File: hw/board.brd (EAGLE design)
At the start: 50 x 50 mm, 21 parts, among them IC2 HS73XX, IC3 DS1820, IC4 DS1820

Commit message: Changes to the board
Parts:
- moved +3.3V 8.89 mm to (2.54, 36.2)
- moved C3 6.35 mm to (5.71, 28.6)
- moved MOTOR 6.35 mm to (2.54, 28.6)
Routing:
- net +3V3: track 143.0 -> 150.0 mm
- net 1Y: track 19.0 -> 24.1 mm
- net 2Y: track 19.0 -> 15.9 mm
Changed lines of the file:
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@@
 <?xml version="1.0" encoding="utf-8"?>
 <!DOCTYPE eagle SYSTEM "eagle.dtd">
-<eagle version="6.6.0">
+<eagle version="7.0.0">
 <drawing>
 <settings>
@@
 <text x="41.91" y="34.925" size="0.8128" layer="25" font="vector" ratio="15" rot="R180" align="center-left">SCL</text>
 <hole x="1.905" y="1.905" drill="2.8"/>
-<text x="4.445" y="26.035" size="0.8128" layer="25" font="vector" ratio="15" align="center-left">+3.3V</text>
-<text x="4.445" y="28.575" size="0.8128" layer="25" font="vector" ratio="15" align="center-left">GND</text>
+<text x="4.445" y="34.925" size="0.8128" layer="25" font="vector" ratio="15" align="center-left">+3.3V</text>
+<text x="4.445" y="37.465" size="0.8128" layer="25" font="vector" ratio="15" align="center-left">GND</text>
 <text x="4.445" y="44.45" size="0.8128" layer="25" font="vector" ratio="15" align="center-left">GND</text>
 <text x="4.445" y="41.91" size="0.8128" layer="25" font="vector" ratio="15" align="center-left">VIN</text>
@@
 <pass name="Default">
 <param name="RoutingGrid" value="50mil"/>
+<param name="AutoGrid" value="1"/>
+<param name="Efforts" value="0"/>
+<param name="TopRouterVariant" value="1"/>
 <param name="tpViaShape" value="round"/>
 <param name="PrefDir.1" value="|"/>
@@
 <attribute name="VALUE" x="35.1536" y="5.08" size="1.27" layer="27" rot="R180"/>
 </element>
-<element name="MOTOR" library="pinhead" package="1X02" value="" x="2.54" y="34.925" smashed="yes" rot="R270">
-<attribute name="NAME" x="3.7338" y="38.6588" size="0.8128" layer="25" font="vector" ratio="15" align="top-center"/>
-<attribute name="VALUE" x="-0.635" y="37.465" size="1.27" layer="27" rot="R270"/>
+<element name="MOTOR" library="pinhead" package="1X02" value="" x="2.54" y="28.575" smashed="yes" rot="R270">
+<attribute name="NAME" x="3.7338" y="32.3088" size="0.8128" layer="25" font="vector" ratio="15" align="top-center"/>
+<attribute name="VALUE" x="-0.635" y="31.115" size="1.27" layer="27" rot="R270"/>
 </element>
 <element name="SERIAL" library="board" package="1X04" value="" x="46.99" y="17.145" smashed="yes" rot="R270">
@@
 <attribute name="VALUE" x="13.208" y="33.147" size="1.27" layer="27" ratio="10" rot="R180"/>
 </element>
-<element name="C3" library="rcl" package="C025-024X044" value="" x="5.715" y="34.925" smashed="yes" rot="R270">
-<attribute name="NAME" x="7.112" y="36.703" size="0.8128" layer="25" font="vector" ratio="15" rot="R270"/>
-<attribute name="VALUE" x="3.048" y="36.703" size="1.27" layer="27" ratio="10" rot="R270"/>
-</element>
-<element name="+3.3V" library="pinhead" package="1X02" value="" x="2.54" y="27.305" smashed="yes" rot="R90">
-<attribute name="VALUE" x="5.715" y="24.765" size="1.27" layer="27" rot="R90"/>
+<element name="C3" library="rcl" package="C025-024X044" value="" x="5.715" y="28.575" smashed="yes" rot="R270">
+<attribute name="NAME" x="7.112" y="30.353" size="0.8128" layer="25" font="vector" ratio="15" rot="R270"/>
+<attribute name="VALUE" x="3.048" y="30.353" size="1.27" layer="27" ratio="10" rot="R270"/>
+</element>
+<element name="+3.3V" library="pinhead" package="1X02" value="" x="2.54" y="36.195" smashed="yes" rot="R90">
+<attribute name="VALUE" x="5.715" y="33.655" size="1.27" layer="27" rot="R90"/>
 </element>
 </elements>
@@
 <via x="40.005" y="40.64" extent="1-16" drill="0.6" shape="square"/>
 <wire x1="21.59" y1="40.64" x2="20.955" y2="40.005" width="0.4064" layer="16"/>
-<wire x1="12.7" y1="30.48" x2="8.89" y2="26.67" width="0.4064" layer="1"/>
-<wire x1="8.89" y1="26.67" x2="8.89" y2="23.495" width="0.4064" layer="1"/>
-<wire x1="8.89" y1="23.495" x2="10.16" y2="22.225" width="0.4064" layer="1"/>
-<wire x1="10.16" y1="22.225" x2="11.43" y2="22.225" width="0.4064" layer="1"/>
 <wire x1="12.7" y1="30.48" x2="12.7" y2="29.21" width="0.4064" layer="1"/>
-<wire x1="12.7" y1="29.21" x2="13.97" y2="27.94" width="0.4064" layer="1"/>
-<wire x1="13.97" y1="27.94" x2="15.24" y2="27.94" width="0.4064" layer="1"/>
+<wire x1="12.7" y1="29.21" x2="11.43" y2="27.94" width="0.4064" layer="1"/>
+<wire x1="11.43" y1="27.94" x2="15.24" y2="27.94" width="0.4064" layer="1"/>
 <via x="15.24" y="27.94" extent="1-16" drill="0.6" shape="square"/>
 <wire x1="15.24" y1="27.94" x2="19.685" y2="27.94" width="0.4064" layer="16"/>
@@
 <wire x1="43.815" y1="29.845" x2="43.815" y2="28.575" width="0.4064" layer="1"/>
 <wire x1="43.815" y1="28.575" x2="44.45" y2="27.94" width="0.4064" layer="1"/>
-<wire x1="4.445" y1="20.955" x2="6.35" y2="20.955" width="0.4064" layer="1"/>
-<wire x1="6.35" y1="20.955" x2="8.89" y2="23.495" width="0.4064" layer="1"/>
+<wire x1="4.445" y1="20.955" x2="6.985" y2="20.955" width="0.4064" layer="1"/>
 <wire x1="31.75" y1="9.525" x2="31.75" y2="8.89" width="0.4064" layer="16"/>
 <wire x1="31.75" y1="8.89" x2="34.925" y2="5.715" width="0.4064" layer="16"/>
 <via x="34.925" y="5.715" extent="1-16" drill="0.6" shape="square"/>
 <contactref element="+3.3V" pad="1"/>
-<wire x1="8.89" y1="26.67" x2="5.715" y2="26.67" width="0.4064" layer="1"/>
-<wire x1="5.715" y1="26.67" x2="5.08" y2="26.035" width="0.4064" layer="1"/>
-<wire x1="5.08" y1="26.035" x2="2.54" y2="26.035" width="0.4064" layer="1"/>
+<wire x1="6.985" y1="20.955" x2="8.255" y2="22.225" width="0.4064" layer="1"/>
+<wire x1="8.255" y1="22.225" x2="11.43" y2="22.225" width="0.4064" layer="1"/>
+<wire x1="8.255" y1="22.225" x2="8.255" y2="27.305" width="0.4064" layer="1"/>
+<wire x1="8.255" y1="27.305" x2="8.89" y2="27.94" width="0.4064" layer="1"/>
+<wire x1="8.89" y1="27.94" x2="11.43" y2="27.94" width="0.4064" layer="1"/>
+<wire x1="2.54" y1="34.925" x2="6.985" y2="34.925" width="0.4064" layer="1"/>
+<wire x1="6.985" y1="34.925" x2="7.62" y2="34.29" width="0.4064" layer="1"/>
+<wire x1="7.62" y1="34.29" x2="7.62" y2="29.21" width="0.4064" layer="1"/>
+<wire x1="7.62" y1="29.21" x2="8.89" y2="27.94" width="0.4064" layer="1"/>
 </signal>
 <signal name="1Y">
@@
 <contactref element="U$1" pad="1"/>
 <contactref element="C3" pad="1"/>
-<wire x1="5.715" y1="36.195" x2="5.715" y2="38.735" width="0.4064" layer="16"/>
-<wire x1="5.715" y1="38.735" x2="7.62" y2="40.64" width="0.4064" layer="16"/>
-<wire x1="7.62" y1="40.64" x2="13.335" y2="40.64" width="0.4064" layer="16"/>
-<wire x1="13.335" y1="40.64" x2="15.875" y2="38.1" width="0.4064" layer="16"/>
-<wire x1="15.875" y1="38.1" x2="17.145" y2="38.1" width="0.4064" layer="16"/>
-<wire x1="5.715" y1="36.195" x2="2.54" y2="36.195" width="0.4064" layer="16"/>
+<wire x1="5.715" y1="29.845" x2="2.54" y2="29.845" width="0.4064" layer="16"/>
+<wire x1="17.145" y1="38.1" x2="15.24" y2="38.1" width="0.4064" layer="16"/>
+<wire x1="15.24" y1="38.1" x2="13.335" y2="40.005" width="0.4064" layer="16"/>
+<wire x1="13.335" y1="40.005" x2="8.255" y2="40.005" width="0.4064" layer="16"/>
+<wire x1="8.255" y1="40.005" x2="7.62" y2="39.37" width="0.4064" layer="16"/>
+<wire x1="7.62" y1="39.37" x2="7.62" y2="31.75" width="0.4064" layer="16"/>
+<wire x1="7.62" y1="31.75" x2="5.715" y2="29.845" width="0.4064" layer="16"/>
 </signal>
 <signal name="2Y">
@@
 <contactref element="U$1" pad="4"/>
 <contactref element="C3" pad="2"/>
-<wire x1="5.715" y1="33.655" x2="2.54" y2="33.655" width="0.4064" layer="16"/>
-<wire x1="5.715" y1="33.655" x2="5.715" y2="31.115" width="0.4064" layer="16"/>
-<wire x1="5.715" y1="31.115" x2="8.255" y2="28.575" width="0.4064" layer="16"/>
-<wire x1="8.255" y1="28.575" x2="13.97" y2="28.575" width="0.4064" layer="16"/>
+<wire x1="5.715" y1="27.305" x2="2.54" y2="27.305" width="0.4064" layer="16"/>
+<wire x1="5.715" y1="27.305" x2="6.985" y2="28.575" width="0.4064" layer="16"/>
+<wire x1="6.985" y1="28.575" x2="13.97" y2="28.575" width="0.4064" layer="16"/>
 <wire x1="13.97" y1="28.575" x2="15.875" y2="30.48" width="0.4064" layer="16"/>
 <wire x1="15.875" y1="30.48" x2="17.145" y2="30.48" width="0.4064" layer="16"/>
@@
 <contactref element="R1" pad="2"/>
 <wire x1="5.715" y1="1.905" x2="9.525" y2="1.905" width="0.254" layer="16"/>
-<wire x1="9.525" y1="1.905" x2="11.43" y2="3.81" width="0.254" layer="16"/>
-<wire x1="11.43" y1="3.81" x2="11.43" y2="6.985" width="0.254" layer="16"/>
-<wire x1="11.43" y1="6.985" x2="12.7" y2="8.255" width="0.254" layer="16"/>
-<wire x1="12.7" y1="8.255" x2="12.7" y2="10.795" width="0.254" layer="16"/>
+<wire x1="9.525" y1="1.905" x2="12.7" y2="5.08" width="0.254" layer="16"/>
+<wire x1="12.7" y1="5.08" x2="12.7" y2="10.795" width="0.254" layer="16"/>
 <wire x1="12.7" y1="10.795" x2="14.605" y2="12.7" width="0.254" layer="16"/>
 <via x="14.605" y="12.7" extent="1-16" drill="0.6" shape="square"/>

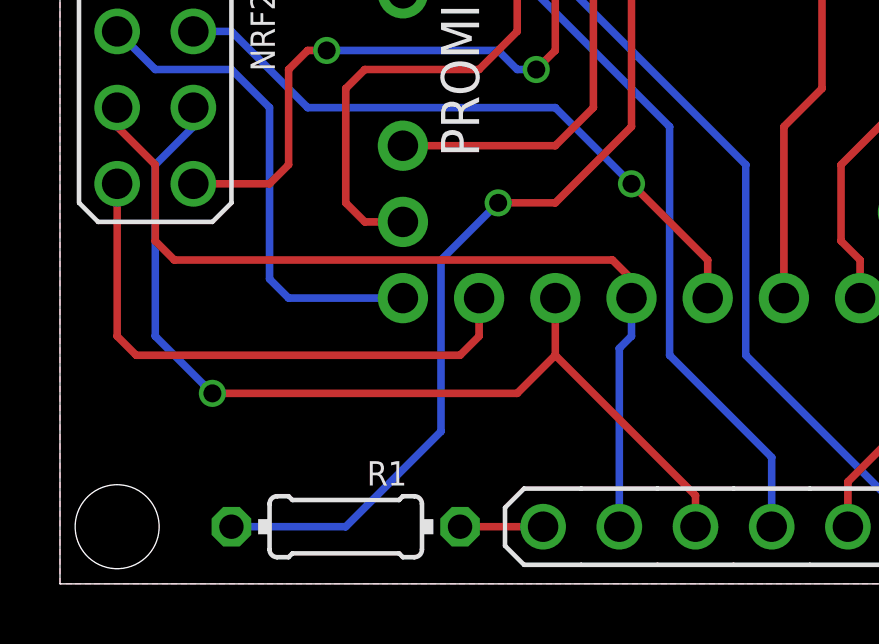
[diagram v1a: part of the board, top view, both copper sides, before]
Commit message: Fixed swapped MISO/MOSI in pcb design. -_-
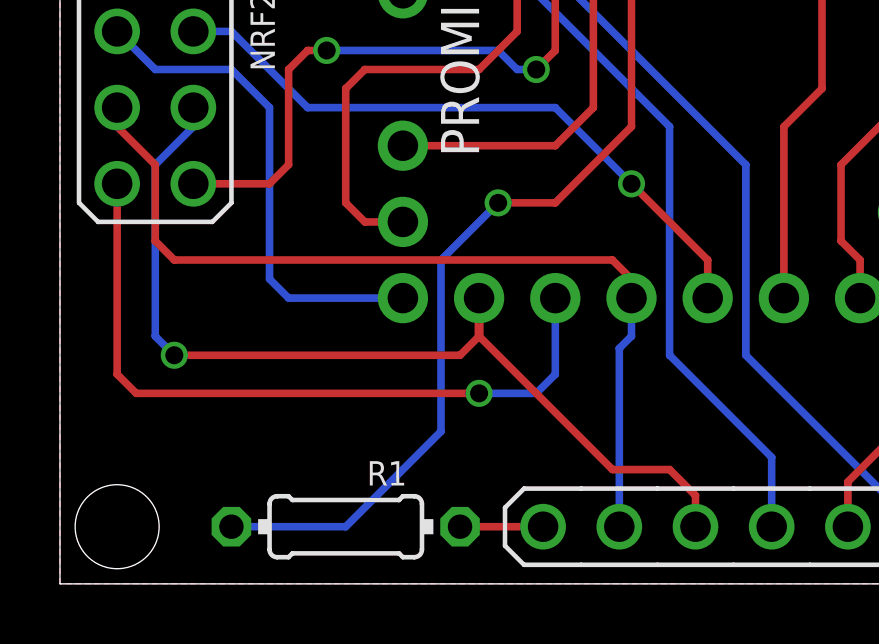
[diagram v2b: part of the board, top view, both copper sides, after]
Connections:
- net MISO: now also PROMINI.15; no longer PROMINI.14
- net MOSI: now also PROMINI.14; no longer PROMINI.15
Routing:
- net MISO: track 18.9 -> 24.0 mm, vias 0 -> 1
- net MOSI: track 32.4 -> 31.2 mm
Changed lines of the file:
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@@
 <?xml version="1.0" encoding="utf-8"?>
 <!DOCTYPE eagle SYSTEM "eagle.dtd">
-<eagle version="7.0.0">
+<eagle version="7.2.0">
 <drawing>
 <settings>
@@
 <contactref element="LCD" pad="6"/>
 <contactref element="NRF24L01" pad="6"/>
-<contactref element="PROMINI" pad="15"/>
 <wire x1="4.445" y1="15.875" x2="4.445" y2="15.24" width="0.254" layer="16"/>
 <wire x1="4.445" y1="15.24" x2="3.175" y2="13.97" width="0.254" layer="16"/>
 <wire x1="3.175" y1="13.97" x2="3.175" y2="8.255" width="0.254" layer="16"/>
-<wire x1="3.175" y1="8.255" x2="5.08" y2="6.35" width="0.254" layer="16"/>
-<via x="5.08" y="6.35" extent="1-16" drill="0.6" shape="square"/>
-<wire x1="5.08" y1="6.35" x2="15.24" y2="6.35" width="0.254" layer="1"/>
-<wire x1="15.24" y1="6.35" x2="16.51" y2="7.62" width="0.254" layer="1"/>
-<wire x1="16.51" y1="7.62" x2="16.51" y2="9.525" width="0.254" layer="1"/>
+<wire x1="3.175" y1="8.255" x2="3.81" y2="7.62" width="0.254" layer="16"/>
+<via x="3.81" y="7.62" extent="1-16" drill="0.6" shape="square"/>
+<wire x1="3.81" y1="7.62" x2="13.335" y2="7.62" width="0.254" layer="1"/>
+<wire x1="13.335" y1="7.62" x2="13.97" y2="8.255" width="0.254" layer="1"/>
 <wire x1="21.1836" y1="1.905" x2="21.1836" y2="2.9464" width="0.254" layer="1"/>
-<wire x1="21.1836" y1="2.9464" x2="16.51" y2="7.62" width="0.254" layer="1"/>
+<wire x1="21.1836" y1="2.9464" x2="20.32" y2="3.81" width="0.254" layer="1"/>
+<wire x1="20.32" y1="3.81" x2="18.415" y2="3.81" width="0.254" layer="1"/>
+<wire x1="18.415" y1="3.81" x2="13.97" y2="8.255" width="0.254" layer="1"/>
+<contactref element="PROMINI" pad="14"/>
+<wire x1="13.97" y1="8.255" x2="13.97" y2="9.525" width="0.3048" layer="1"/>
 </signal>
 <signal name="SCK">
@@
 <signal name="MISO">
 <contactref element="NRF24L01" pad="7"/>
-<contactref element="PROMINI" pad="14"/>
-<wire x1="1.905" y1="13.335" x2="1.905" y2="8.255" width="0.254" layer="1"/>
-<wire x1="1.905" y1="8.255" x2="2.54" y2="7.62" width="0.254" layer="1"/>
-<wire x1="2.54" y1="7.62" x2="13.335" y2="7.62" width="0.254" layer="1"/>
-<wire x1="13.335" y1="7.62" x2="13.97" y2="8.255" width="0.254" layer="1"/>
-<wire x1="13.97" y1="8.255" x2="13.97" y2="9.525" width="0.254" layer="1"/>
+<contactref element="PROMINI" pad="15"/>
+<wire x1="1.905" y1="13.335" x2="1.905" y2="6.985" width="0.254" layer="1"/>
+<wire x1="1.905" y1="6.985" x2="2.54" y2="6.35" width="0.254" layer="1"/>
+<wire x1="2.54" y1="6.35" x2="13.97" y2="6.35" width="0.254" layer="1"/>
+<via x="13.97" y="6.35" extent="1-16" drill="0.6" shape="square"/>
+<wire x1="13.97" y1="6.35" x2="15.875" y2="6.35" width="0.254" layer="16"/>
+<wire x1="16.51" y1="6.985" x2="16.51" y2="9.525" width="0.254" layer="16"/>
+<wire x1="15.875" y1="6.35" x2="16.51" y2="6.985" width="0.254" layer="16"/>
 </signal>
 <signal name="+3V3">
